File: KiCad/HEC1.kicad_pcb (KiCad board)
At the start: 2 copper layers, 243.8 x 170.2 mm, 655 parts, among them J1 Barrel_Jack_Switch, J2 Conn_02x12_Odd_Even, J3 Conn_02x05_Odd_Even, J5 Screw_Terminal_01x02, J6 DE9_Plug_MountingHoles, J7 AudioJack3, J8 NES_Port_Male, J9 Conn_02x14_Odd_Even, SW1 SW_DIP_x04, SW2 SW_Push, U1 Z80CPU, U10 74LS32, U11 74LS00, U12 74LS04, U13 74LS245, U14 74LS245, U15 74LS32, U16 74LS32, U17 74LS20, U18 74LS138, U19 74LS30, U2 AS6C4008-55PCN, U20 74LS574, U21 74LS574, U22 74LS02, U23 74LS74, U24 74LS74, U25 74LS541, U26 74LS541, U27 74LS74, U28 74LS30, U29 74LS74, U3 AS6C4008-55PCN, U30 74LS74, U31 74LS32, U32 LM79M05_TO220, U33 74LS20, U34 74LS393, U35 74LS08, U36 74LS574, U37 74LS32, U38 74LS47, U39 74LS47, U4 CY7C199, U40 DA04-11EWA, U41 74LS02, U42 74LS06, U44 74LS541, U5 CY7C199, U6 74LS138, U7 28C256, U8 74LS138, U9 74LS574, X1 CXO_DIP8, Y1 Crystal

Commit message: Bug fixes
fixed some bugs introduced to the schematic. More routing.
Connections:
- J2 pad 10: /HEC_Peripherals/D0 -> /HEC_IO/D0
- J2 pad 12: /HEC_Peripherals/~{RESET} -> /HEC_CPU/~{RESET}
- J2 pad 3: /HEC_Peripherals/D7 -> /HEC_IO/D7
- J2 pad 4: /HEC_Peripherals/D6 -> /HEC_IO/D6
- J2 pad 5: /HEC_Peripherals/D5 -> /HEC_IO/D5
- J2 pad 6: /HEC_Peripherals/D4 -> /HEC_IO/D4
- J2 pad 7: /HEC_Peripherals/D3 -> /HEC_IO/D3
- J2 pad 8: /HEC_Peripherals/D2 -> /HEC_IO/D2
- J2 pad 9: /HEC_Peripherals/D1 -> /HEC_IO/D1
- U10 pad 4: unconnected-(U10-Pad4) -> /HEC_Memory/ATTR_RI
- U2 pad 24: /HEC_Memory/~{RAM_OE} -> /HEC_IO/~{IOR}
- U3 pad 24: /HEC_Memory/~{RAM_OE} -> /HEC_IO/~{IOR}
- U37 pad 11: /HEC_Memory/~{RAM_OE} -> /HEC_IO/~{IOR}
- U43 pad 12: /HEC_Peripherals/D0 -> /HEC_IO/D0
- U43 pad 13: /HEC_Peripherals/D1 -> /HEC_IO/D1
- U43 pad 14: /HEC_Peripherals/D2 -> /HEC_IO/D2
- U43 pad 15: /HEC_Peripherals/D3 -> /HEC_IO/D3
- U43 pad 16: /HEC_Peripherals/D4 -> /HEC_IO/D4
- U43 pad 17: /HEC_Peripherals/D5 -> /HEC_IO/D5
- U43 pad 18: /HEC_Peripherals/D6 -> /HEC_IO/D6
- U43 pad 19: /HEC_Peripherals/D7 -> /HEC_IO/D7
- U43 pad 4: /HEC_Peripherals/~{RESET} -> /HEC_CPU/~{RESET}
- U44 pad 11: /HEC_Peripherals/D7 -> /HEC_IO/D7
- U44 pad 12: /HEC_Peripherals/D6 -> /HEC_IO/D6
- U44 pad 13: /HEC_Peripherals/D5 -> /HEC_IO/D5
- U44 pad 14: /HEC_Peripherals/D4 -> /HEC_IO/D4
- U44 pad 15: /HEC_Peripherals/D3 -> /HEC_IO/D3
- U44 pad 16: /HEC_Peripherals/D2 -> /HEC_IO/D2
- U44 pad 17: /HEC_Peripherals/D1 -> /HEC_IO/D1
- U44 pad 18: /HEC_Peripherals/D0 -> /HEC_IO/D0
- U6 pad 5: /HEC_IO/~{IORQ} -> /HEC_CPU/~{IORQ}
- U9 pad 12: /HEC_Memory/SYSGATE -> /HEC_Memory/PROC_ID2
- U9 pad 13: /HEC_Memory/PROC_ID6 -> /HEC_Memory/PROC_ID3
- U9 pad 14: /HEC_Memory/PROC_ID5 -> /HEC_Memory/PROC_ID1
- U9 pad 15: /HEC_Memory/PROC_ID4 -> /HEC_Memory/PROC_ID0
- U9 pad 16: /HEC_Memory/PROC_ID3 -> /HEC_Memory/PROC_ID4
- U9 pad 17: /HEC_Memory/PROC_ID2 -> /HEC_Memory/PROC_ID5
- U9 pad 18: /HEC_Memory/PROC_ID1 -> /HEC_Memory/PROC_ID6
- U9 pad 19: /HEC_Memory/PROC_ID0 -> /HEC_Memory/SYSGATE
- U9 pad 2: /HEC_IO/D0 -> /HEC_IO/D7
- U9 pad 3: /HEC_IO/D1 -> /HEC_IO/D6
- U9 pad 4: /HEC_IO/D2 -> /HEC_IO/D5
- U9 pad 5: /HEC_IO/D3 -> /HEC_IO/D4
- U9 pad 6: /HEC_IO/D4 -> /HEC_IO/D0
- U9 pad 7: /HEC_IO/D5 -> /HEC_IO/D1
- U9 pad 8: /HEC_IO/D6 -> /HEC_IO/D3
- U9 pad 9: /HEC_IO/D7 -> /HEC_IO/D2
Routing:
- net /HEC_IO/~{IO_CS4}: track 0.00 -> 86.8 mm, vias 0 -> 2
- net L: track 683.5 -> 766.9 mm
- net /HEC_CPU/~{RESET}: track 99.1 -> 177.2 mm, vias 0 -> 1
- net /HEC_IO/D7: track 310.1 -> 387.0 mm
- net H: track 622.6 -> 690.0 mm
- net /HEC_Memory/~{RAM_OE}: track 58.5 -> 0.00 mm
- net /HEC_IO/~{IOR}: track 119.0 -> 177.5 mm
- net /HEC_IO/~{IRQ1}: track 5.08 -> 61.1 mm
- net /HEC_IO/A2: track 135.2 -> 190.7 mm
- net /HEC_IO/D0: track 254.2 -> 306.7 mm, vias 4 -> 5
- net /HEC_IO/A3: track 153.5 -> 205.5 mm
- net /HEC_IO/D6: track 290.7 -> 342.2 mm
- net /HEC_IO/D5: track 266.7 -> 317.1 mm
- net /HEC_IO/~{IO_CS5}: track 0.00 -> 48.0 mm, vias 0 -> 1
- net /HEC_IO/~{IO_CS6}: track 0.00 -> 46.3 mm, vias 0 -> 1
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
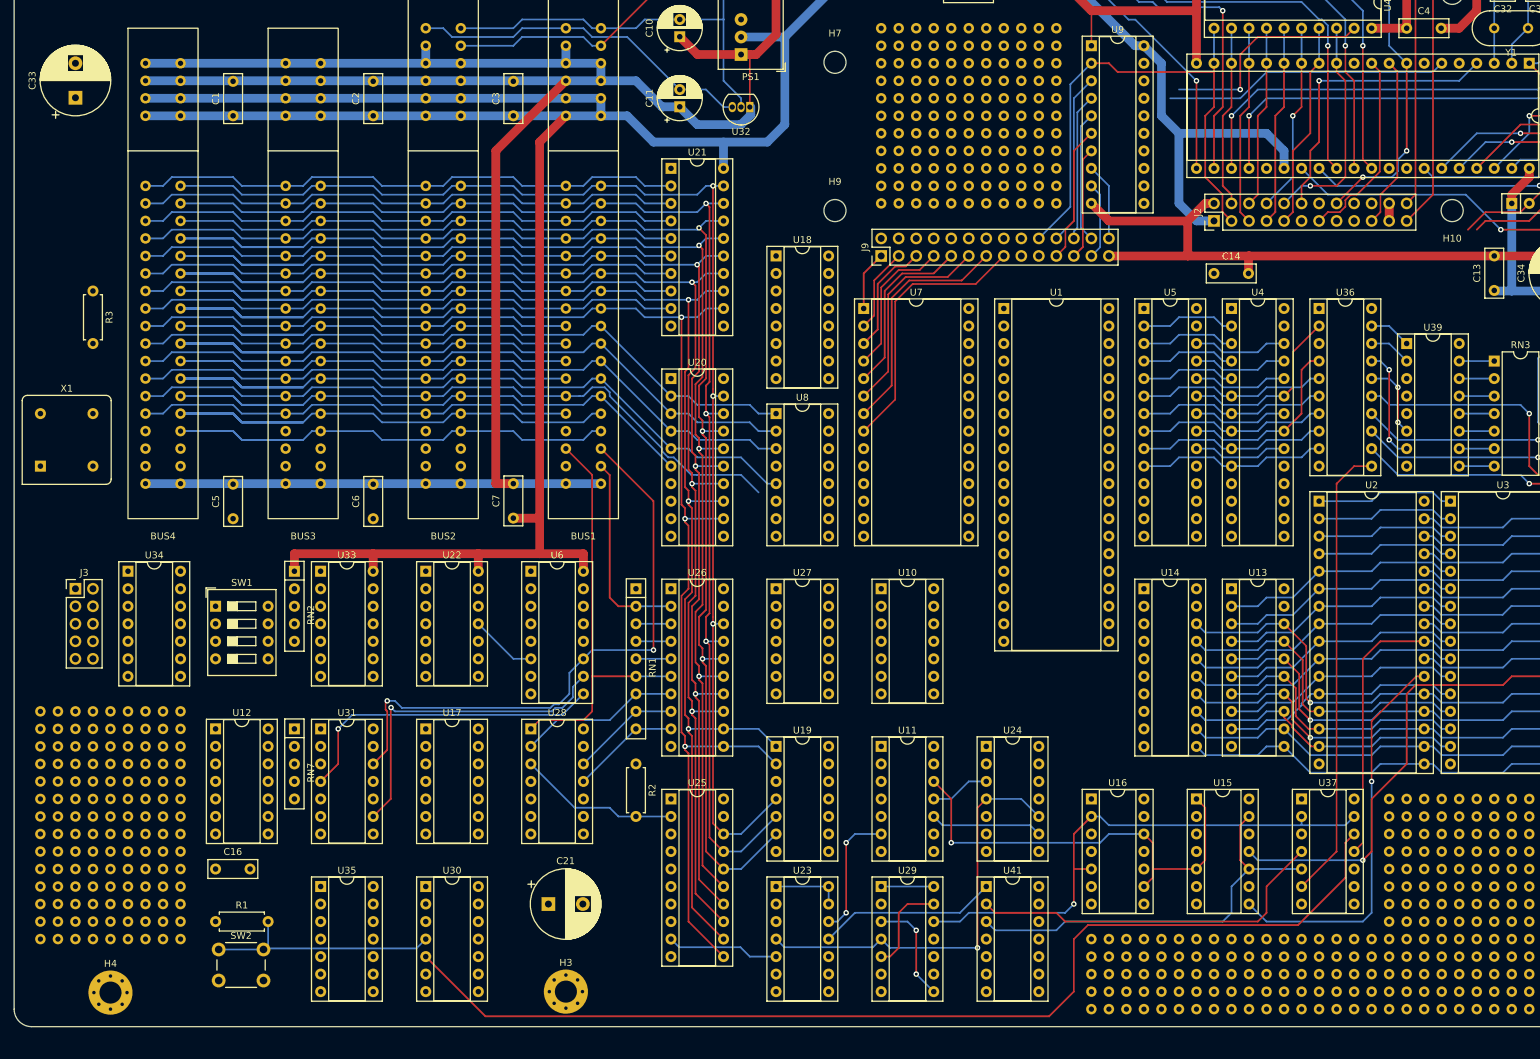
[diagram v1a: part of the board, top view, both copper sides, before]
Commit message: More routing, a power LED
Did some easier routing. The current concern is that the already done easy routing would take up space for harder to route traces, making them even harder. However, one have to start somewhere... The power LED is added to assist debugging.
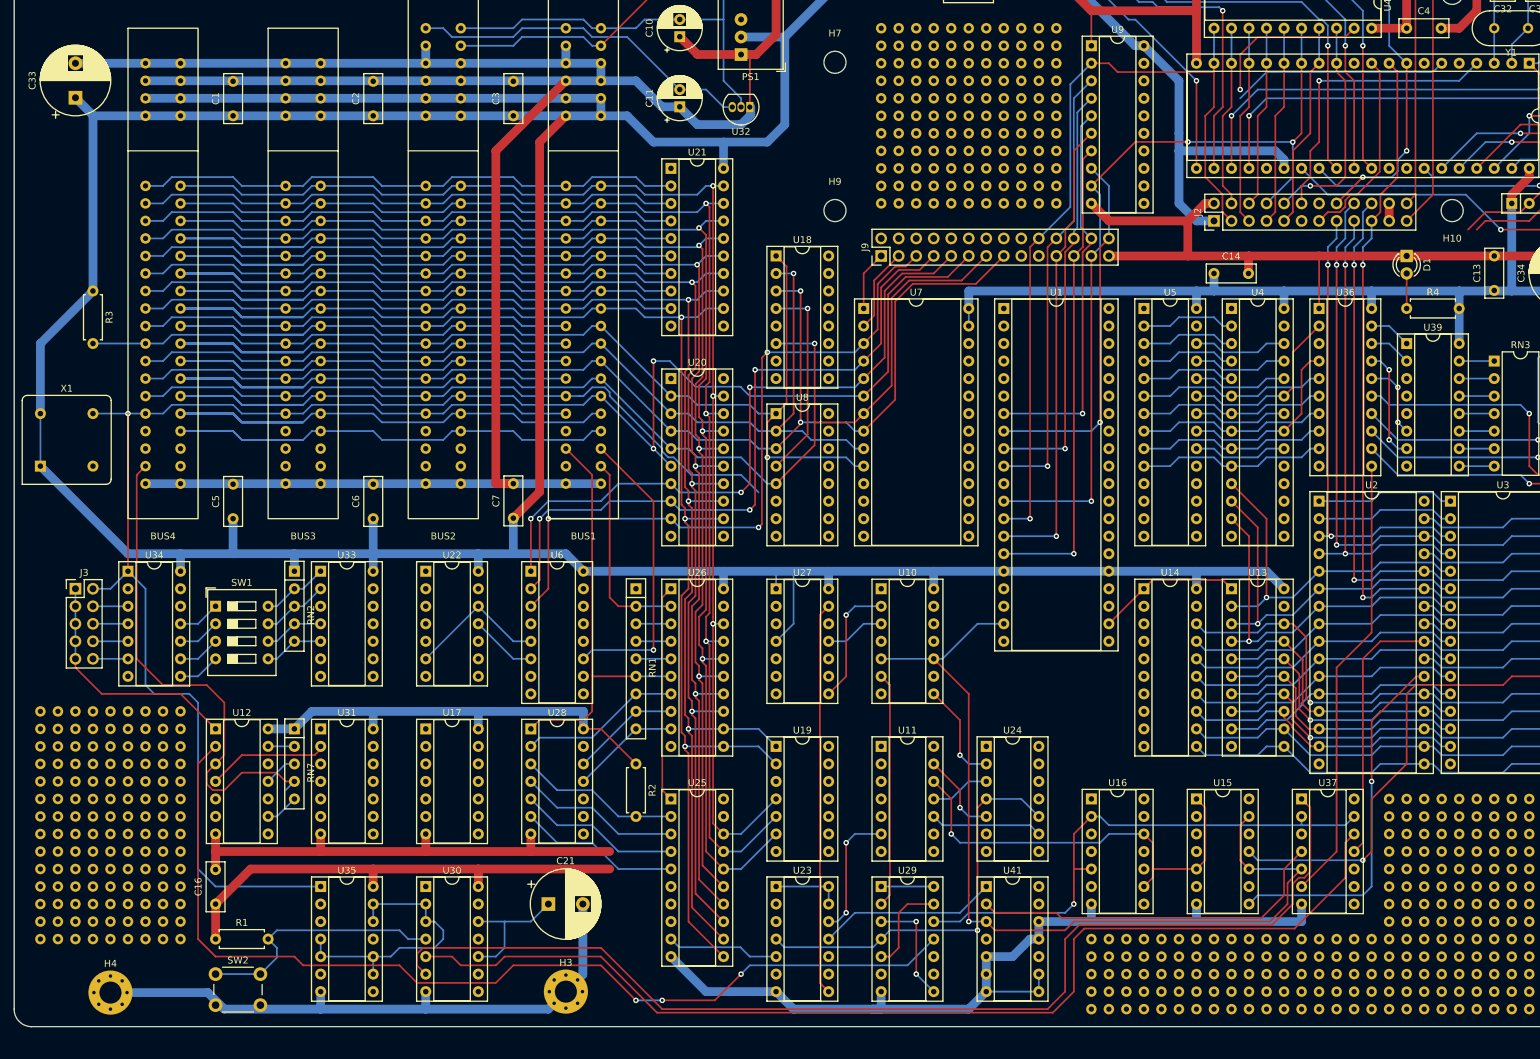
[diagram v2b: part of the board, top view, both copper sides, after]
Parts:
- added D1: LED, LED_THT:LED_D3.0mm, F.Cu at (236.2, 83.8)
- added R4: R, Resistor_THT:R_Axial_DIN0207_L6.3mm_D2.5mm_P7.62mm_Horizontal, F.Cu at (236.2, 91.4)
- moved C16 5.08 mm to (63.5, 177.8), turned to 90 degrees
- moved SW2 3.60 mm to (63.5, 188.0)
- moved R1 2.54 mm to (63.5, 182.9)
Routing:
- net H: track 690.0 -> 1183.2 mm
- net L: track 766.9 -> 1108.4 mm
- net Net-(U30A-~{Q}): track 0.00 -> 162.6 mm
- net Net-(U29B-C): track 0.00 -> 145.1 mm, vias 0 -> 3
- net /HEC_IO/A0: track 194.7 -> 304.7 mm, vias 0 -> 3
- net /HEC_IO/A1: track 169.8 -> 276.3 mm, vias 0 -> 3
- net /HEC_IO/OSC: track 64.1 -> 169.9 mm, vias 0 -> 1
- net /HEC_IO/A3: track 205.5 -> 305.2 mm, vias 0 -> 3
- net /HEC_IO/A4: track 165.4 -> 257.1 mm, vias 0 -> 4
- net /HEC_IO/A2: track 190.7 -> 277.0 mm, vias 0 -> 4
- net /HEC_IO/A7: track 36.9 -> 122.0 mm, vias 0 -> 3
- net /HEC_IO/D2: track 295.0 -> 375.1 mm, vias 5 -> 7
- net /HEC_IO/A6: track 41.3 -> 121.0 mm, vias 0 -> 3
- net /HEC_IO/A5: track 45.8 -> 119.4 mm, vias 0 -> 3
- net /HEC_IO/~{NOWS4}: track 0.00 -> 73.1 mm
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
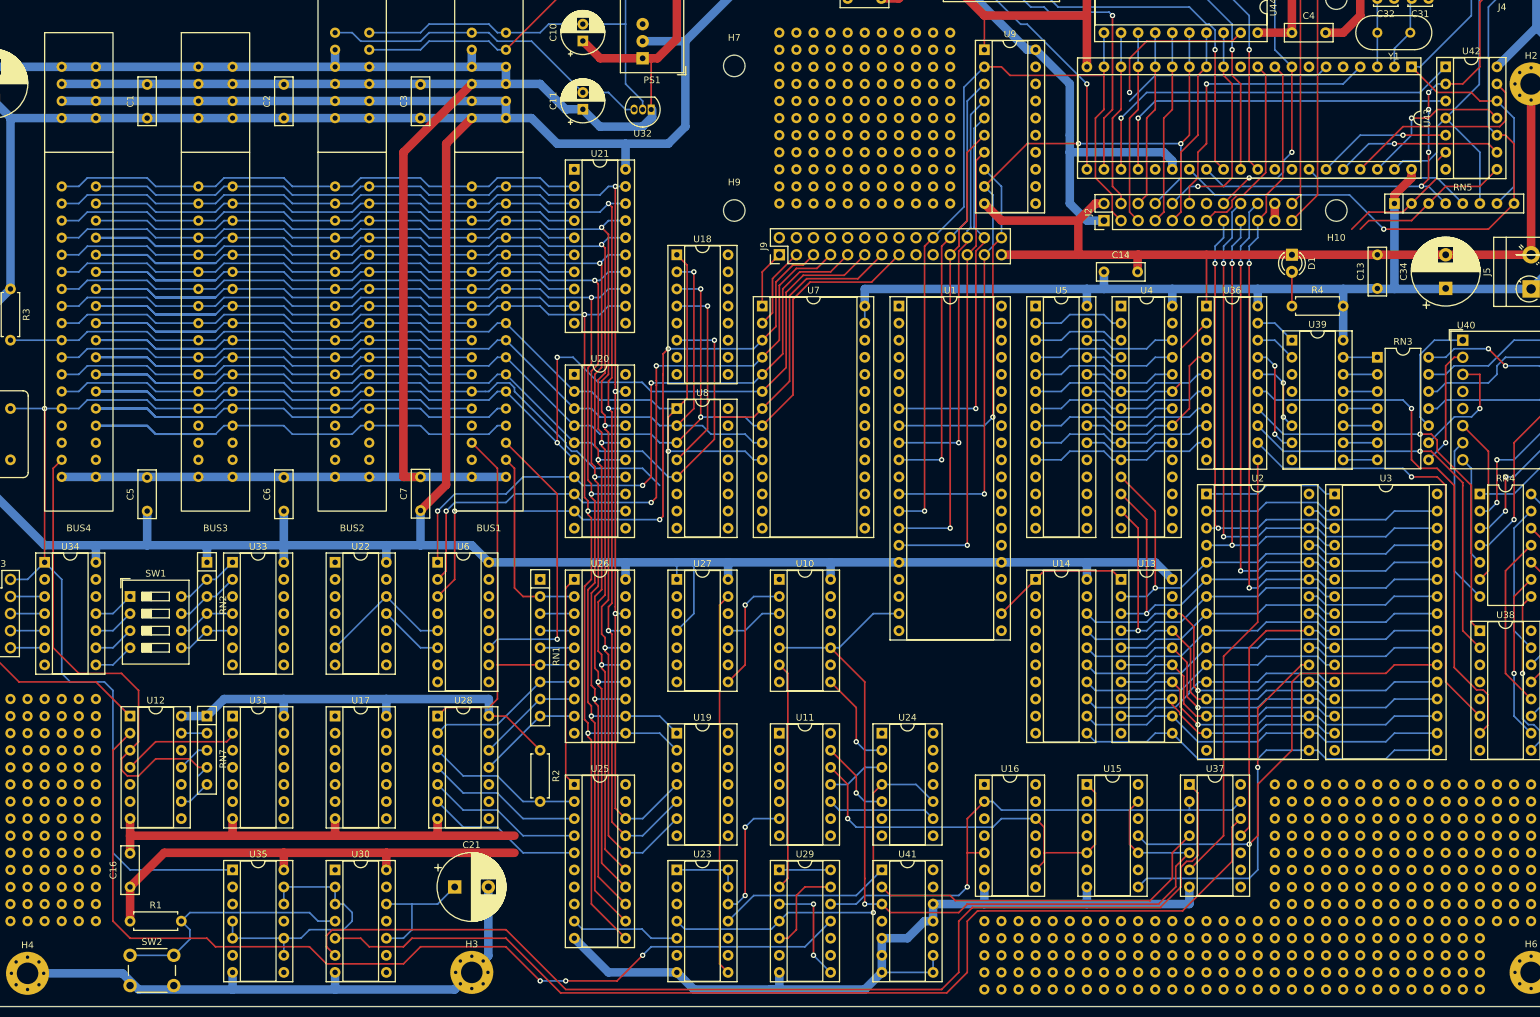
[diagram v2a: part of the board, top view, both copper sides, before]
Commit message: More routing
Even more routing... Maybe 50% finished? The remaining 50% is probably harder though.
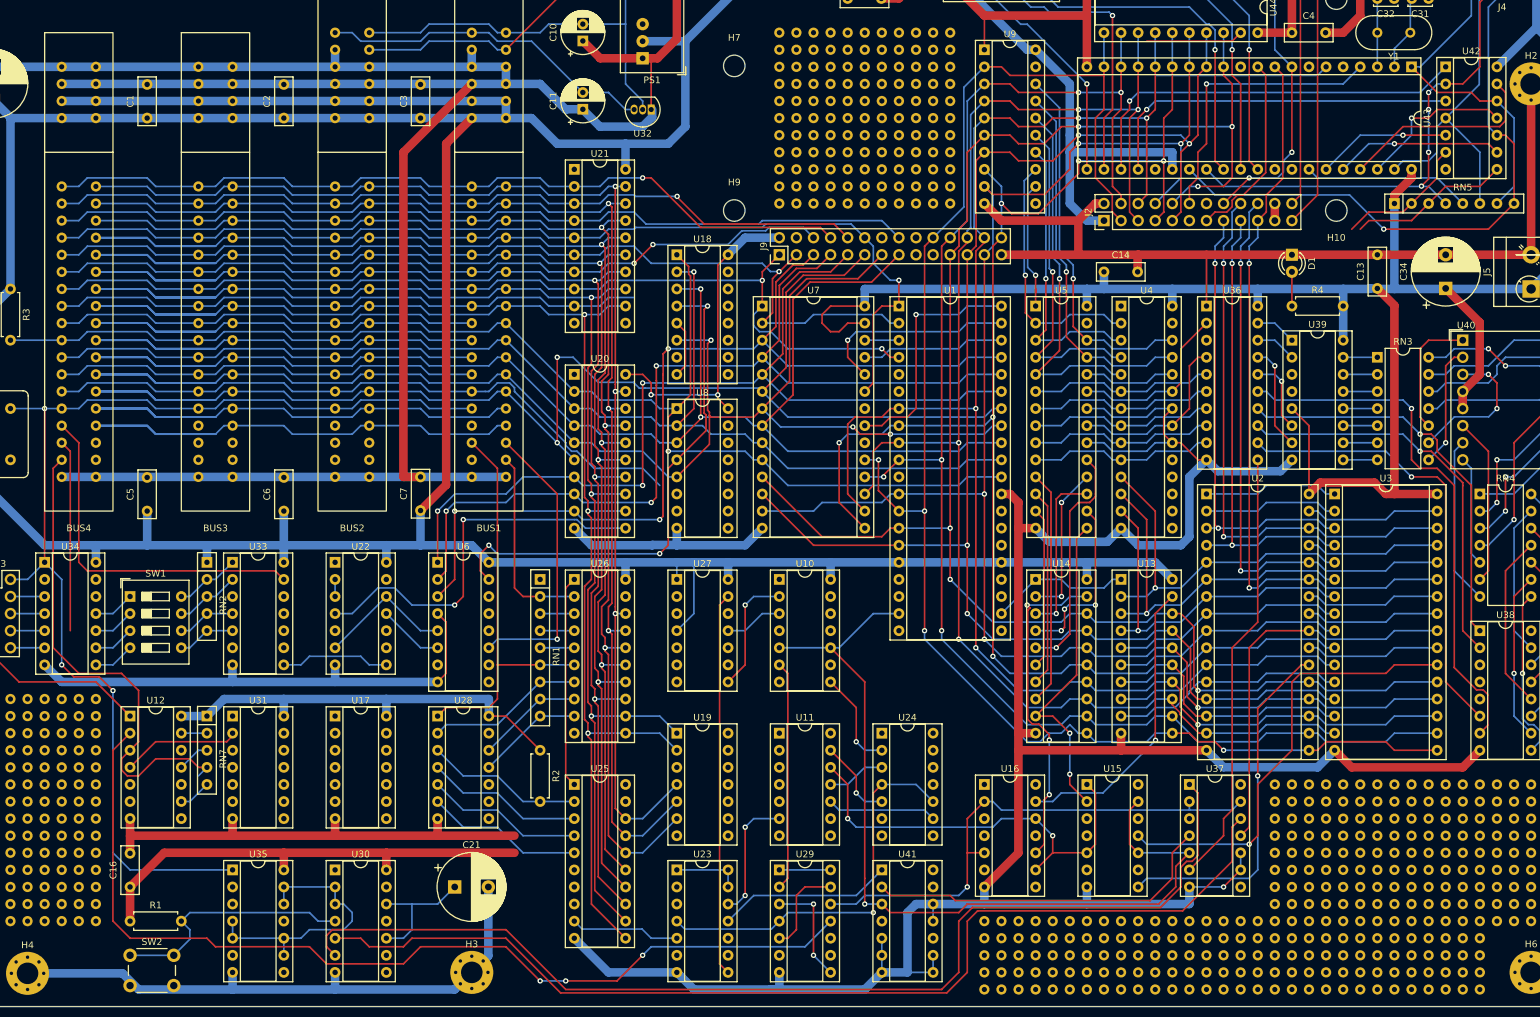
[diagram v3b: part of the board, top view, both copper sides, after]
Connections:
- U4 pad 1: /HEC_Memory/PROC_ID0 -> /HEC_Memory/PROC_ID2
- U4 pad 2: /HEC_Memory/PROC_ID1 -> /HEC_Memory/PROC_ID3
- U4 pad 3: /HEC_Memory/PROC_ID2 -> /HEC_Memory/PROC_ID1
- U4 pad 4: /HEC_Memory/PROC_ID3 -> /HEC_Memory/PROC_ID0
- U5 pad 1: /HEC_Memory/PROC_ID0 -> /HEC_Memory/PROC_ID2
- U5 pad 2: /HEC_Memory/PROC_ID1 -> /HEC_Memory/PROC_ID3
- U5 pad 3: /HEC_Memory/PROC_ID2 -> /HEC_Memory/PROC_ID1
- U5 pad 4: /HEC_Memory/PROC_ID3 -> /HEC_Memory/PROC_ID0
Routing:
- net L: track 1108.4 -> 1449.0 mm, vias 0 -> 1
- net H: track 1183.2 -> 1332.5 mm, vias 0 -> 2
- net /HEC_IO/D3: track 330.9 -> 435.4 mm, vias 4 -> 9
- net /HEC_IO/D4: track 347.0 -> 450.0 mm, vias 5 -> 8
- net /HEC_IO/D0: track 355.7 -> 449.7 mm, vias 6 -> 9
- net /HEC_IO/D5: track 357.0 -> 444.5 mm, vias 4 -> 7
- net /HEC_IO/A10: track 94.2 -> 180.8 mm, vias 0 -> 1
- net /HEC_IO/D1: track 340.2 -> 426.8 mm, vias 4 -> 7
- net /HEC_IO/D6: track 382.1 -> 463.2 mm, vias 4 -> 8
- net /HEC_IO/A11: track 107.9 -> 182.1 mm, vias 0 -> 1
- net /HEC_IO/A9: track 106.4 -> 180.3 mm, vias 0 -> 2
- net /HEC_IO/A8: track 107.2 -> 170.8 mm, vias 0 -> 1
- net /HEC_IO/D2: track 375.1 -> 437.3 mm, vias 7 -> 8
- net /HEC_IO/D7: track 432.0 -> 492.9 mm, vias 4 -> 7
- net Net-(U20-Cp): track 0.00 -> 58.3 mm, vias 0 -> 2
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
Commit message: Livestream commit
Committing live! Just to make sure that I don't lose 1 day of work.
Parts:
- removed the REF** at (45.7, 152.4)
- removed the REF** at (58.4, 152.4)
- removed the REF** at (50.8, 152.4)
- removed the REF** at (58.4, 149.9)
- removed the REF** at (53.3, 152.4)
- removed the REF** at (55.9, 149.9)
- removed the REF** at (43.2, 149.9)
- removed the REF** at (53.3, 149.9)
- removed the REF** at (45.7, 149.9)
- removed the REF** at (48.3, 152.4)
- removed the REF** at (38.1, 152.4)
- removed the REF** at (50.8, 149.9)
- removed the REF** at (38.1, 149.9)
- removed the REF** at (55.9, 152.4)
- removed the REF** at (43.2, 152.4)
- removed the REF** at (40.6, 149.9)
- removed the REF** at (48.3, 149.9)
- removed the REF** at (40.6, 152.4)
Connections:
- U10 pad 12: L -> H
- U10 pad 13: L -> H
- U11 pad 10: /HEC_Protection/~{XFAULT} -> /HEC_Protection/~{WFAULT}
- U11 pad 11: Net-(U24A-C) -> Net-(U24B-C)
- U11 pad 12: /HEC_CPU/~{WR} -> /HEC_Protection/M1
- U11 pad 13: /HEC_Protection/~{WFAULT} -> /HEC_Protection/~{XFAULT}
- U11 pad 8: Net-(U24B-C) -> Net-(U24A-C)
- U11 pad 9: /HEC_Protection/M1 -> /HEC_CPU/~{WR}
- U12 pad 5: /HEC_Protection/~{M1} -> L
- U12 pad 6: /HEC_Protection/M1 -> unconnected-(U12-Pad6)
- U17 pad 10: /HEC_Protection/~{XFAULT} -> /HEC_Protection/~{RFAULT}
- U17 pad 9: /HEC_Protection/~{RFAULT} -> /HEC_Protection/~{XFAULT}
- U22 pad 1: /HEC_Memory/~{RAM_A19} -> unconnected-(U22-Pad1)
- U22 pad 2: /HEC_Memory/RAM_A19 -> H
- U22 pad 3: /HEC_Memory/RAM_A19 -> H
- U41 pad 10: unconnected-(U41-Pad10) -> /HEC_Memory/~{RAM_A19}
- U41 pad 12: L -> /HEC_Protection/~{M1}
- U41 pad 13: unconnected-(U41-Pad13) -> /HEC_Protection/M1
- U41 pad 9: L -> /HEC_Memory/RAM_A19
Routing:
- net /HEC_IO/AUDIO_R: track 126.0 -> 322.2 mm
- net /HEC_IO/AUDIO_L: track 116.1 -> 308.0 mm, vias 0 -> 2
- net H: track 1332.5 -> 1452.0 mm, vias 2 -> 1
- net /HEC_IO/~{NOWS1}: track 4.86 -> 106.0 mm, vias 0 -> 1
- net /HEC_CPU/~{IOPORT_L}: track 0.00 -> 84.8 mm
- net /HEC_Protection/~{RFAULT}: track 13.8 -> 97.1 mm, vias 0 -> 2
- net /HEC_CPU/~{IOPORT_H}: track 0.00 -> 78.0 mm
- net /HEC_IO/~{NOWS2}: track 4.86 -> 76.3 mm, vias 0 -> 1
- net Net-(U34B-CP): track 0.00 -> 66.2 mm, vias 0 -> 1
- net /HEC_IO/~{ROM_OE}: track 64.1 -> 128.8 mm
- net /HEC_IO/~{IO_CS7}: track 0.00 -> 60.9 mm, vias 0 -> 1
- net /HEC_IO/~{SENSE4}: track 5.08 -> 64.0 mm, vias 0 -> 1
- net /HEC_IO/A15: track 117.3 -> 176.3 mm, vias 0 -> 3
- net /HEC_IO/~{WAIT1}: track 0.00 -> 58.3 mm, vias 0 -> 1
- net /HEC_Protection/~{INT_SOURCE_1}: track 0.00 -> 55.8 mm, vias 0 -> 1
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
